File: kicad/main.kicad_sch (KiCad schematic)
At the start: 43 parts, among them M1 TP4056_MODULE, M2 BOOST_MODULE, Q1 AO3407, Q2 2N3904, SW1 SW_Push, U1 LM431, U2 Arduino_pro_mini

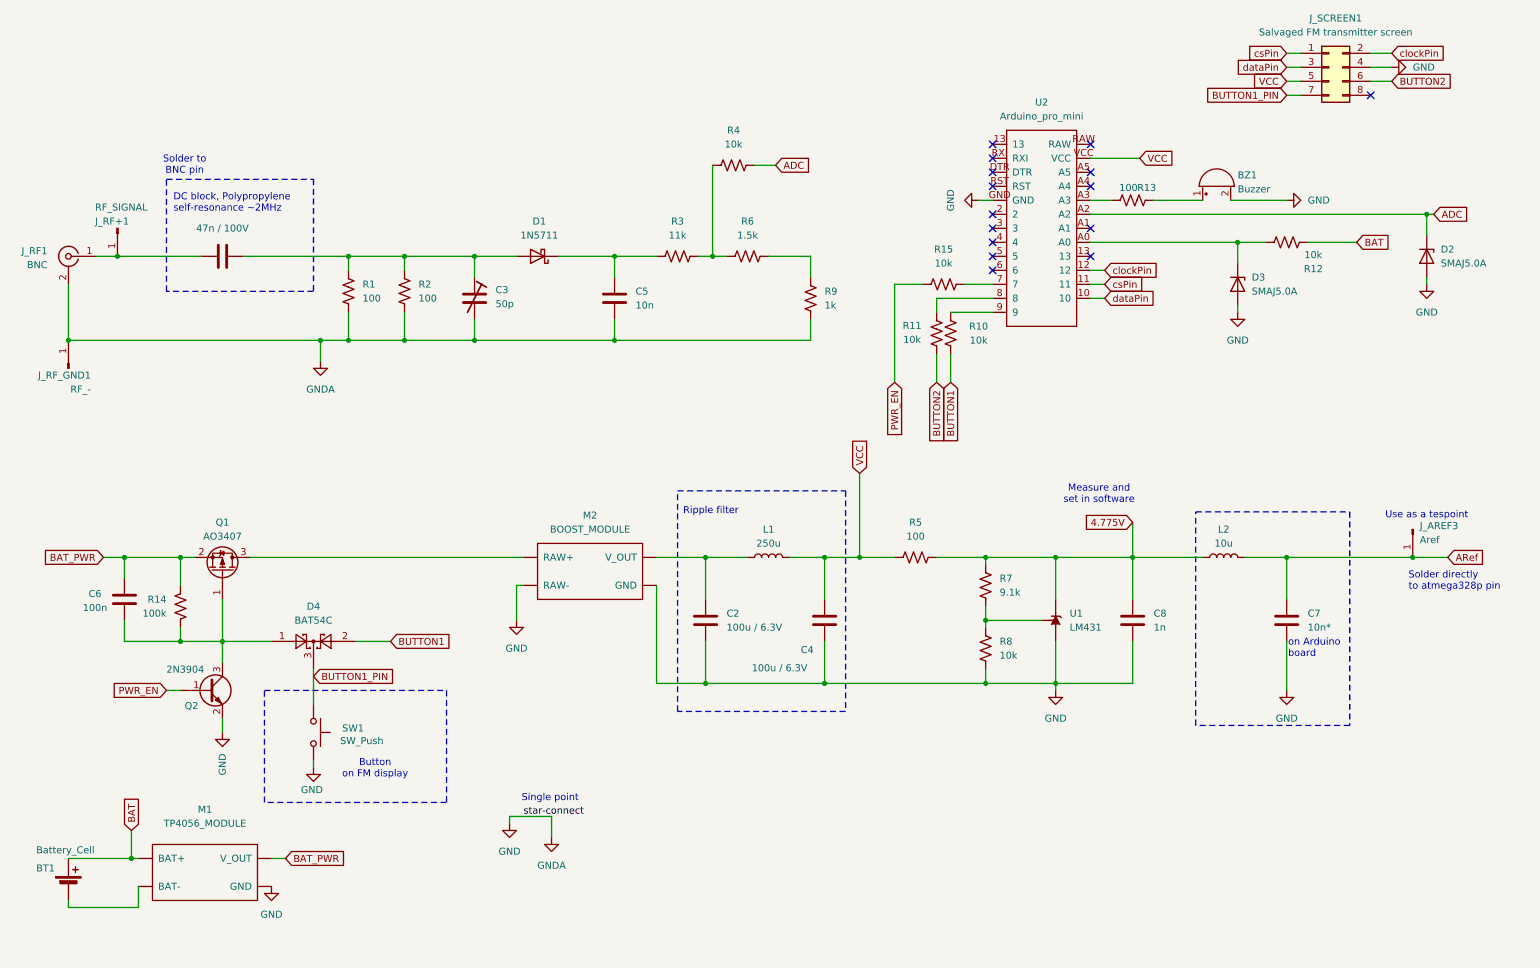
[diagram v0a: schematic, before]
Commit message: docs: clean up schematic and export to pdf and images
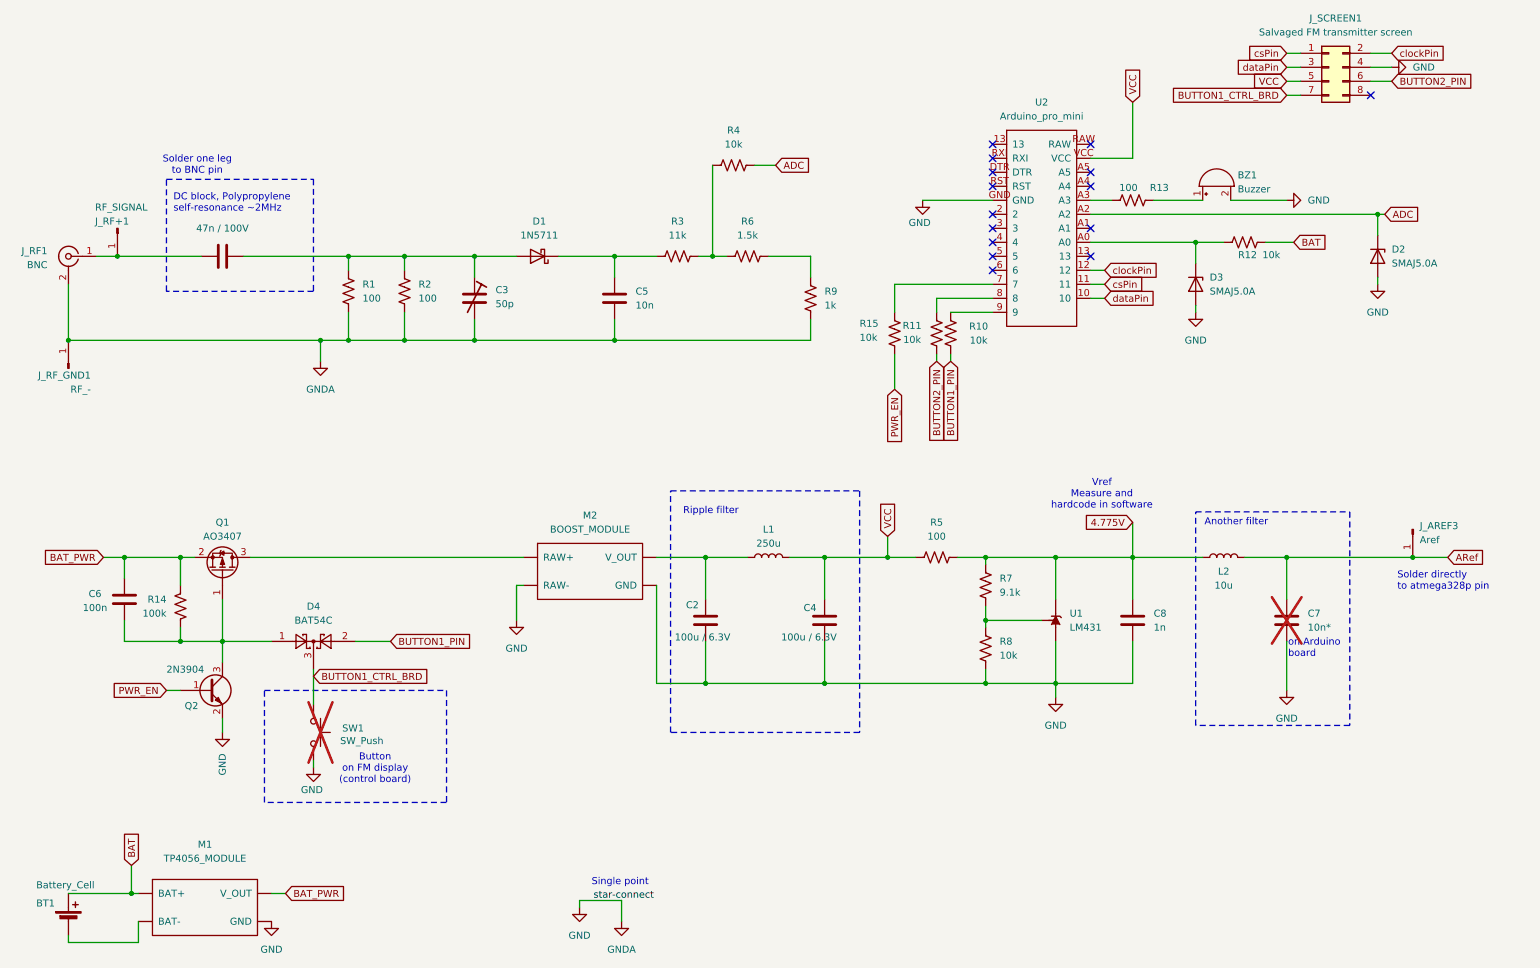
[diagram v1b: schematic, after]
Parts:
- C7, SW1: now not fitted
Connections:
- net BUTTON1 is gone; now on net BUTTON1_PIN: D4.2, R10.2
- net BUTTON1_PIN: no longer D4.3, J_SCREEN1.7 (Pin_7), SW1.1
- net BUTTON2 renamed BUTTON2_PIN
- new net BUTTON1_CTRL_BRD: D4.3, J_SCREEN1.7 (Pin_7), SW1.1
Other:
- note added: "Another filter"
- note added: "Button on FM display (control board)"
- note added: "Solder one leg to BNC pin"
- note added: "Vref Measure and hardcode in software"
- note removed: "Button on FM display"
- note removed: "Measure and set in software"
- note removed: "Solder to BNC pin"
- note removed: "Use as a tespoint"
- moved on the sheet: BT1, D2, D3, M1, R12, R15, R5
